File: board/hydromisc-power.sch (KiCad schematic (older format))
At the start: 39 parts, among them CN1 DC_COAX_POWER_NO_SHIELD, IC1 LM2596, IC3 LM2596, IC7 AZ1117I-LDO

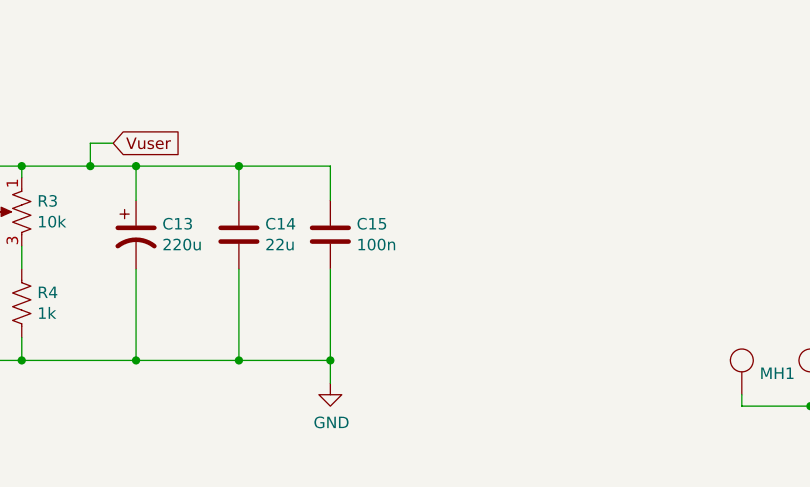
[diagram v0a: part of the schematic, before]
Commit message: Update PCB to rev B.
Add the missing pull-up on ESP32_EN, some pull-down on Vuser to
fight off-brand LM2596 leakage current, and a README.md explaining.
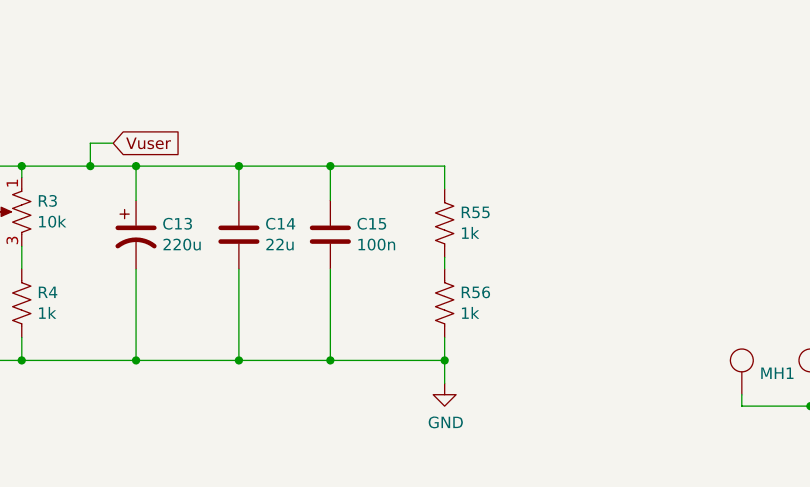
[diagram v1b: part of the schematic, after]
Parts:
- added R55, R56: 1k, hydromisc:HM_0603, symbol Device:R_US
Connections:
- net GND: now also R56.2
- net Vuser: now also R55.1
- new net: R55.2, R56.1
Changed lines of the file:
@@
 Wire Wire Line
 	2800 5350 2800 4850
-Connection ~ 4650 5350
-Wire Wire Line
-	4650 5450 4650 5350
+Wire Wire Line
+	5150 5450 5150 5350
 $Comp
 L power:GND #PWR0105
 U 1 1 603436AE
-P 4650 5450
-F 0 "#PWR0105" H 4650 5200 50  0001 C CNN
-F 1 "GND" H 4655 5277 50  0000 C CNN
-F 2 "" H 4650 5450 50  0001 C CNN
-F 3 "" H 4650 5450 50  0001 C CNN
-	1    4650 5450
+P 5150 5450
+F 0 "#PWR0105" H 5150 5200 50  0001 C CNN
+F 1 "GND" H 5155 5277 50  0000 C CNN
+F 2 "" H 5150 5450 50  0001 C CNN
+F 3 "" H 5150 5450 50  0001 C CNN
+	1    5150 5450
 	1    0    0    -1
 $EndComp
@@
 Wire Wire Line
 	7050 5550 6750 5550
+$Comp
+L Device:R_US R55
+U 1 1 60ECE9DD
+P 5150 4750
+F 0 "R55" H 5218 4796 50  0000 L CNN
+F 1 "1k" H 5218 4705 50  0000 L CNN
+F 2 "hydromisc:HM_0603" V 5190 4740 50  0001 C CNN
+F 3 "~" H 5150 4750 50  0001 C CNN
+	1    5150 4750
+	1    0    0    -1
+$EndComp
+$Comp
+L Device:R_US R56
+U 1 1 60ECF2EC
+P 5150 5100
+F 0 "R56" H 5218 5146 50  0000 L CNN
+F 1 "1k" H 5218 5055 50  0000 L CNN
+F 2 "hydromisc:HM_0603" V 5190 5090 50  0001 C CNN
+F 3 "~" H 5150 5100 50  0001 C CNN
+	1    5150 5100
+	1    0    0    -1
+$EndComp
+Wire Wire Line
+	5150 5350 4650 5350
+Connection ~ 4650 5350
+Wire Wire Line
+	4650 4500 5150 4500
+Wire Wire Line
+	5150 4500 5150 4600
+Connection ~ 4650 4500
+Wire Wire Line
+	5150 4900 5150 4950
+Wire Wire Line
+	5150 5250 5150 5350
+Connection ~ 5150 5350
 $EndSCHEMATC
